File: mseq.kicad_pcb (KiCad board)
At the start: 2 copper layers, 100 x 67 mm, 66 parts, among them J1 Screen_I2C, J2 TC2030-NL, P1 USB_C_Plug_USB2.0, SW1 RESET, SW2 ON/OFF, SW3 MS/SLAVE, SW4 BOOT, U1 SN74AHCT125DR, U2 H11L1M, U3 MCP1703Ax-330xxTT, U4 STM32F413CHUx, U5 CP2102N-Axx-xQFN20, Y1 32.768kHz 6pF, Y2 25MHz 18pF

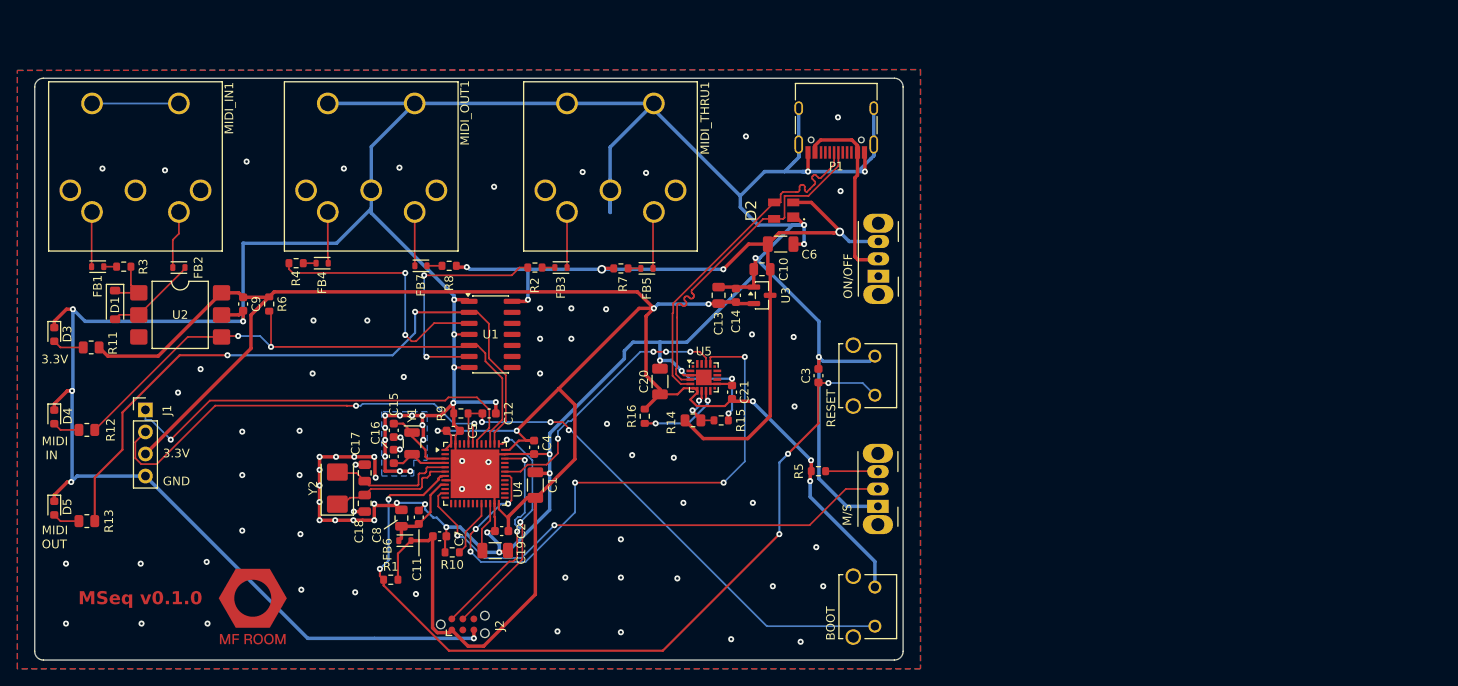
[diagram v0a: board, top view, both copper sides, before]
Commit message: SPI memories wired, AMS1117 regulator, schematic fixes
Add the NOR flash and FRAM to a shared SPI2 bus and clean up the
issues a full schematic review turned up.

Memories (U7 W25Q16JV, U8 MB85RS256B) share SCK/MOSI/MISO on
PB13/PB15/PB14 with separate chip selects on PB12 (NOR) and PB10
(FRAM), each with a 10k pull-up so both stay deselected through
reset. /WP and /HOLD tied high on both parts. QUADSPI is not
bonded out on the 48-pin STM32F413CHU6, so this is single SPI;
the FRAM sets the bus ceiling at 25 MHz for READ.

Regulator U3 moved from MCP1703A (SOT-23A) to AMS1117-3.3
(SOT-223). The SOT-23A's 336 C/W thermal resistance left almost
no margin at the ~166 mA peak load; SOT-223 removes the concern.
C13 accordingly goes 1uF -> 22uF and C10 1uF -> 10uF, since the
AMS1117 needs at least 10uF at VOUT for loop compensation where
the MCP1703A was stable from 1uF.

Also:
- Tie off U1 pins 9/10/12/13, the floating inputs on the two
  unused 74HCT125 buffer channels
- Correct U1 value to SN74HCT125DR to match the ordered part
- Assign missing footprints on U8, R17, R18; fill in BOM fields
- Exclude two ERC warnings on U7 /WP and /HOLD: the symbol
  declares them bidirectional for quad mode, unreachable here

ERC is clean: 0 errors, 0 warnings, 2 exclusions. PCB updated
from schematic; placement and routing not started.

Co-Authored-By: Claude Opus 5 <noreply@anthropic.com>
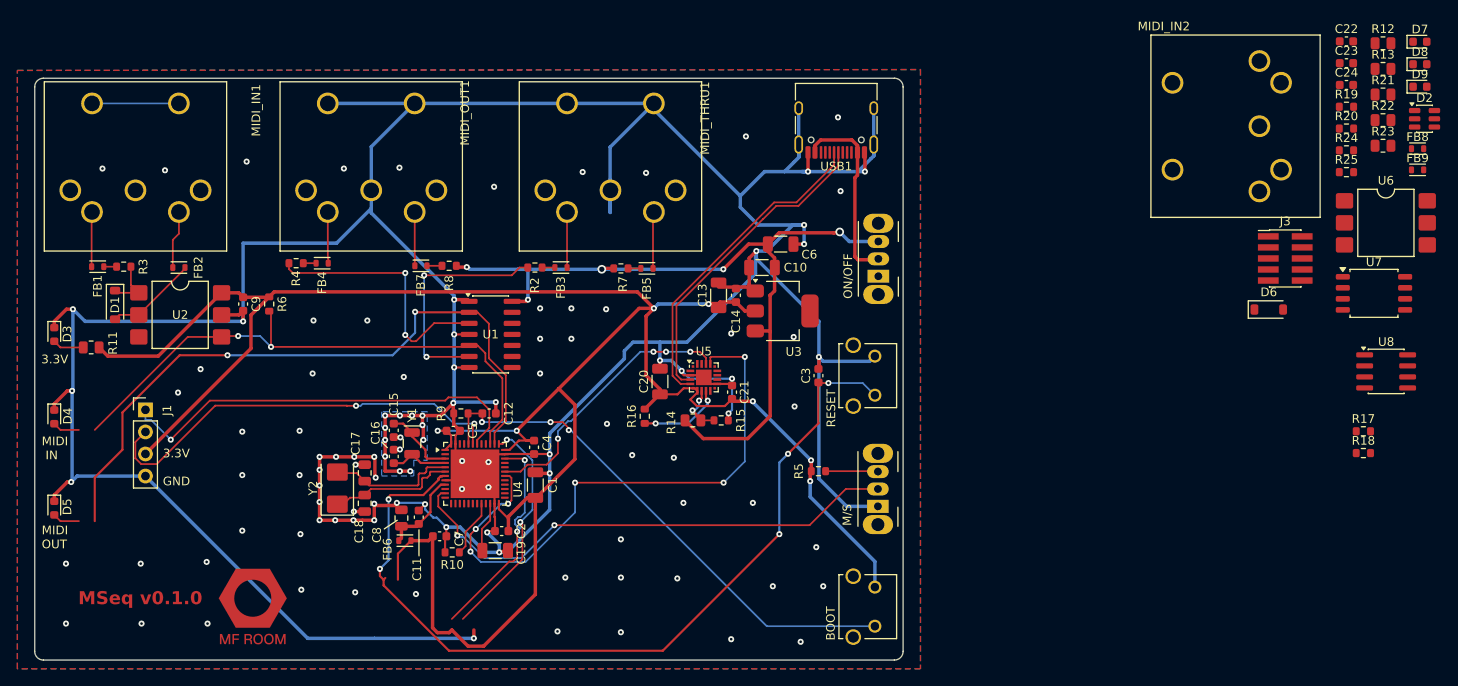
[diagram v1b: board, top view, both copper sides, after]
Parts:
- removed J2: TC2030-NL, Connector:Tag-Connect_TC2030-IDC-NL_2x03_P1.27mm_Vertical
- removed P1: USB_C_Plug_USB2.0, Connector_USB:USB_C_Receptacle_HRO_TYPE-C-31-M-12
- removed R1: 10k, Resistor_SMD:R_0603_1608Metric
- added C22: 100nF, Capacitor_SMD:C_0603_1608Metric, F.Cu at (201.1, 43.8)
- added C23: 100nF, Capacitor_SMD:C_0603_1608Metric, F.Cu at (201.1, 46.3)
- added C24: 100nF, Capacitor_SMD:C_0603_1608Metric, F.Cu at (201.1, 48.8)
- added D6: 1N4148, Diode_SMD:D_SOD-123, F.Cu at (192.1, 74.6)
- added D7: B_LED, LED_SMD:LED_0603_1608Metric, F.Cu at (209.5, 43.8)
- added D8: O_LED, LED_SMD:LED_0603_1608Metric, F.Cu at (209.5, 46.4)
- added D9: O_LED, LED_SMD:LED_0603_1608Metric, F.Cu at (209.5, 49.0)
- added FB8: 1 kΩ @ 100 MHz, Inductor_SMD:L_TDK_MLZ1608, F.Cu at (209.2, 56.1)
- added FB9: 1 kΩ @ 100 MHz, Inductor_SMD:L_TDK_MLZ1608, F.Cu at (209.2, 58.5)
- added J3: Conn_ARM_JTAG_SWD_10, Connector_PinHeader_1.27mm:PinHeader_2x05_P1.27mm_Vertical_SMD, F.Cu at (194.0, 68.8)
- added MIDI_IN2: DIN-5_180degree, mseq_lib:DIN-504, F.Cu at (186.0, 53.5)
- added R17: 5.1K, Resistor_SMD:R_0603_1608Metric, F.Cu at (203.0, 88.7)
- added R18: 5.1K, Resistor_SMD:R_0603_1608Metric, F.Cu at (203.0, 91.2)
- added R19: 220R, Resistor_SMD:R_0603_1608Metric, F.Cu at (201.1, 51.3)
- added R20: 330R, Resistor_SMD:R_0603_1608Metric, F.Cu at (201.1, 53.8)
- added R21: 1KR, Resistor_SMD:R_0805_2012Metric, F.Cu at (205.3, 49.9)
- added R22: 1KR, Resistor_SMD:R_0805_2012Metric, F.Cu at (205.3, 52.8)
- added R23: 1KR, Resistor_SMD:R_0805_2012Metric, F.Cu at (205.3, 55.8)
- added R24: 10k, Resistor_SMD:R_0603_1608Metric, F.Cu at (201.1, 56.3)
- added R25: 10k, Resistor_SMD:R_0603_1608Metric, F.Cu at (201.1, 58.8)
- added U6: H11L1M, Package_DIP:SMDIP-6_W9.53mm, F.Cu at (205.6, 64.7)
- added U7: W25Q16JVSS, Package_SO:SOIC-8_5.3x5.3mm_P1.27mm, F.Cu at (204.2, 72.8)
- added U8: MB85RS256B, Package_SO:SOIC-8_3.9x4.9mm_P1.27mm, F.Cu at (205.6, 81.8)
- added USB1: USB_C_Receptacle_USB2.0_16P, Connector_USB:USB_C_Receptacle_HRO_TYPE-C-31-M-12, F.Cu at (142.3, 52.5)
- C10: value 1uF -> 10uF; footprint Capacitor_SMD:C_0805_2012Metric -> Capacitor_SMD:C_1206_3216Metric
- C13: value 1uF -> 22uF; footprint Capacitor_SMD:C_0805_2012Metric -> Capacitor_SMD:C_1206_3216Metric
- D2: value SP0503BAHTG -> SP0505BAHT; footprint mseq_lib:SOT-143_4 -> Package_TO_SOT_SMD:SOT-23-6
- R11, R12, R13: value 470R -> 1KR
- U1: value SN74AHCT125DR -> SN74HCT125DR
- U3: value MCP1703Ax-330xxTT -> AMS1117-3.3; footprint Package_TO_SOT_SMD:SOT-23 -> Package_TO_SOT_SMD:SOT-223-3_TabPin2
- Y1: value 32.768kHz 6pF -> 32.768kHz ±20ppm 6pF
- Y2: value 25MHz 18pF -> 25 MHz ±20ppm 18pF
- moved R13 158.1 mm to (205.3, 46.9), turned to 0 degrees
- moved R12 155.8 mm to (205.3, 44.0), turned to 0 degrees
- moved D2 74.5 mm to (210.0, 52.7), turned to 0 degrees
- moved U3 2.98 mm to (136.1, 74.8)
- moved C10 0.20 mm to (133.8, 69.8)
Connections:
- D2 pad 1: GND -> Net-(USB1-CC1)
- D2 pad 2: VBUS -> GND
- D2 pad 3: /D- -> Net-(USB1-CC2)
- D2 pad 4: /D+ -> VBUS
- D4 pad 1: GND -> /B3
- D5 pad 1: GND -> /A15
- MIDI_IN1 pad 2: unconnected-(MIDI_IN1-GND-PadG1) -> unconnected-(MIDI_IN1-Pad2)
- MIDI_IN1 pad G1: unconnected-(MIDI_IN1-GND-PadG1) -> (no net)
- MIDI_IN1 pad G2: unconnected-(MIDI_IN1-GND-PadG1) -> (no net)
- MIDI_OUT1 pad 4: Net-(FB4-Pad1) -> Net-(FB7-Pad2)
- MIDI_OUT1 pad 5: Net-(FB7-Pad2) -> Net-(FB4-Pad1)
- MIDI_OUT1 pad G1: GND -> (no net)
- MIDI_OUT1 pad G2: GND -> (no net)
- MIDI_THRU1 pad 4: Net-(FB3-Pad1) -> Net-(FB5-Pad2)
- MIDI_THRU1 pad 5: Net-(FB5-Pad2) -> Net-(FB3-Pad1)
- MIDI_THRU1 pad G1: GND -> (no net)
- MIDI_THRU1 pad G2: GND -> (no net)
- R12 pad 1: /B3 -> +3.3V
- R13 pad 1: /A15 -> +3.3V
- U1 pad 10: unconnected-(U1-Pad10) -> GND
- U1 pad 12: unconnected-(U1-Pad12) -> GND
- U1 pad 13: unconnected-(U1-Pad13) -> GND
- U1 pad 9: unconnected-(U1-Pad9) -> GND
- U4 pad 13: unconnected-(U4-PA3-Pad13) -> /A3
- U4 pad 21: unconnected-(U4-PB10-Pad21) -> /CSFRAM
- U4 pad 25: unconnected-(U4-PB12-Pad25) -> /CSNOR
- U4 pad 26: unconnected-(U4-PB13-Pad26) -> /SCK
- U4 pad 27: unconnected-(U4-PB14-Pad27) -> /MISO
- U4 pad 28: unconnected-(U4-PB15-Pad28) -> /MOSI
- U5 pad 19: unconnected-(U5-~{RXT}/GPIO.3-Pad19) -> /RXT
- U5 pad 20: unconnected-(U5-~{TXT}/GPIO.2-Pad20) -> /TXT
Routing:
- net unconnected-(MIDI_IN1-GND-PadG1): track 10.00 -> 0.00 mm
- net (no net): track 0.00 -> 10.00 mm
- net VBUS: track 97.7 -> 93.2 mm
- net /D+: track 39.5 -> 36.0 mm
- net /D-: track 39.7 -> 36.7 mm
- net GND: track 552.3 -> 554.2 mm
- net +3.3V: track 269.5 -> 270.2 mm
